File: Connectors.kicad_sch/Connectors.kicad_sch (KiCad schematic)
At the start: 4 parts, among them J1 I2C, J2 GPIO, J3 Serial, J4 ISCP

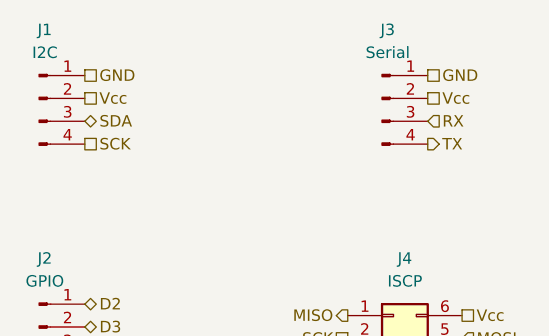
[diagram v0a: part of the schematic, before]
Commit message: Have added required symbols to the schematic sheets.
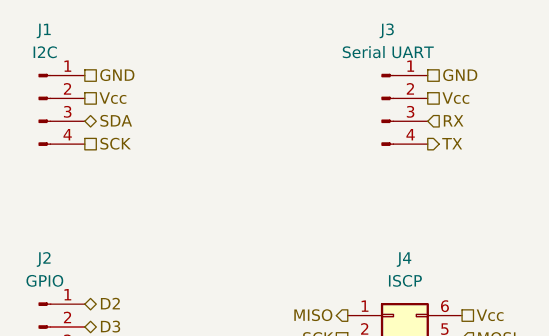
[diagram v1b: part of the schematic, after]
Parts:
- J3: value Serial -> Serial UART
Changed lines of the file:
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@@
 			)
 		)
-		(property "Value" "Serial"
+		(property "Value" "Serial UART"
 			(at 158.115 73.66 0)
 			(effects

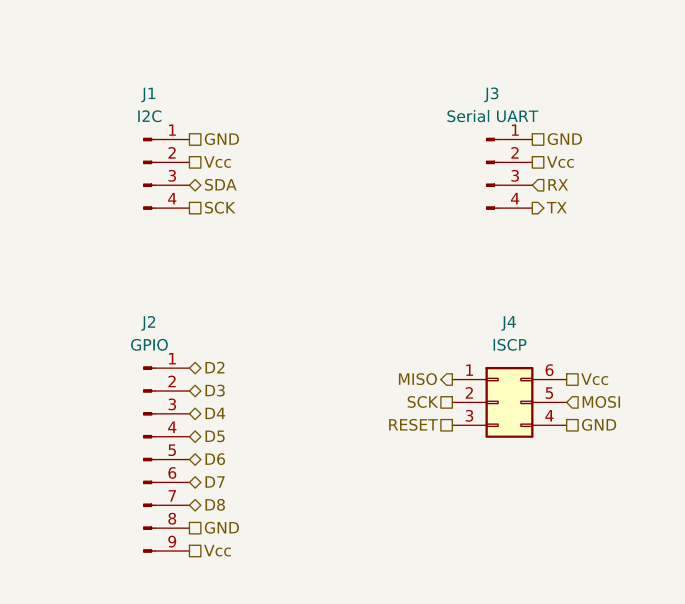
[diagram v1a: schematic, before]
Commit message: Added component values.
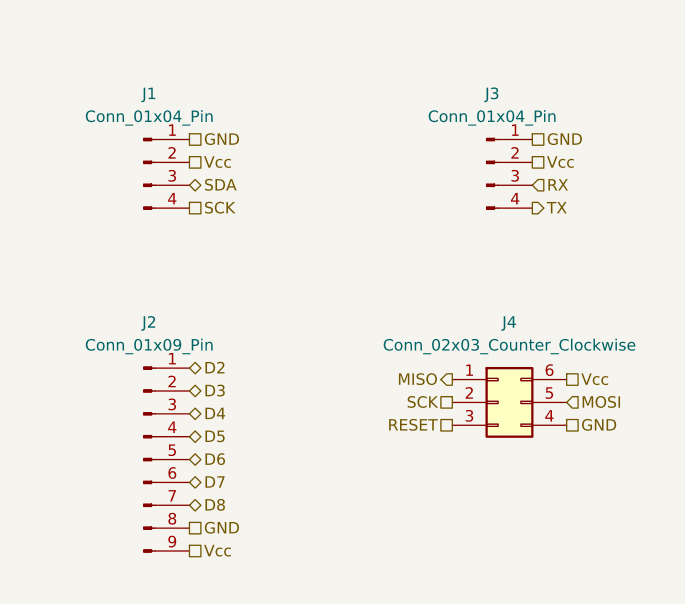
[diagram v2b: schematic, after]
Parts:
- J1: value I2C -> Conn_01x04_Pin
- J2: value GPIO -> Conn_01x09_Pin
- J3: value Serial UART -> Conn_01x04_Pin
- J4: value ISCP -> Conn_02x03_Counter_Clockwise
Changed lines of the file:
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@@
 	)
 	(symbol
+		(lib_name "Conn_02x03_Counter_Clockwise_1")
 		(lib_id "Connector_Generic:Conn_02x03_Counter_Clockwise")
 		(at 158.75 105.41 0)
@@
 			)
 		)
-		(property "Value" "ISCP"
+		(property "Value" "Conn_02x03_Counter_Clockwise"
 			(at 160.02 99.06 0)
 			(effects
@@
 			)
 		)
+		(pin "6"
+		)
+		(pin "3"
+		)
+		(pin "5"
+		)
+		(pin "1"
+		)
 		(pin "4"
 		)
-		(pin "5"
-		)
-		(pin "1"
-		)
 		(pin "2"
 		)
-		(pin "6"
-		)
-		(pin "3"
-		)
 		(instances
-			(project "KiCAD_Proj (MCU datalogger)"
+			(project ""
 				(path "/4bd39814-648a-43e5-9d59-9775154104be/332bdd2b-acd5-4556-89bc-1329fd5879e3"
 					(reference "J4")
@@
 	)
 	(symbol
-		(lib_name "Conn_01x04_Pin_1")
+		(lib_name "Conn_01x04_Pin_2")
 		(lib_id "Connector:Conn_01x04_Pin")
-		(at 130.81 74.93 0)
+		(at 157.48 78.74 0)
 		(unit 1)
 		(exclude_from_sim no)
@@
 		(on_board yes)
 		(dnp no)
+		(fields_autoplaced yes)
+		(property "Reference" "J3"
+			(at 158.115 71.12 0)
+			(effects
+				(font
+					(size 1.27 1.27)
+				)
+			)
+		)
+		(property "Value" "Conn_01x04_Pin"
+			(at 158.115 73.66 0)
+			(effects
+				(font
+					(size 1.27 1.27)
+				)
+			)
+		)
+		(property "Footprint" ""
+			(at 157.48 78.74 0)
+			(effects
+				(font
+					(size 1.27 1.27)
+				)
+				(hide yes)
+			)
+		)
+		(property "Datasheet" "~"
+			(at 157.48 78.74 0)
+			(effects
+				(font
+					(size 1.27 1.27)
+				)
+				(hide yes)
+			)
+		)
+		(property "Description" "Generic connector, single row, 01x04, script generated"
+			(at 157.48 78.74 0)
+			(effects
+				(font
+					(size 1.27 1.27)
+				)
+				(hide yes)
+			)
+		)
+		(pin "3"
+		)
+		(pin "2"
+		)
+		(pin "4"
+		)
+		(pin "1"
+		)
+		(instances
+			(project ""
+				(path "/4bd39814-648a-43e5-9d59-9775154104be/332bdd2b-acd5-4556-89bc-1329fd5879e3"
+					(reference "J3")
+					(unit 1)
+				)
+			)
+		)
+	)
+	(symbol
+		(lib_name "Conn_01x04_Pin_3")
+		(lib_id "Connector:Conn_01x04_Pin")
+		(at 119.38 78.74 0)
+		(unit 1)
+		(exclude_from_sim no)
+		(in_bom yes)
+		(on_board yes)
+		(dnp no)
+		(fields_autoplaced yes)
 		(property "Reference" "J1"
 			(at 120.015 71.12 0)
@@
 			)
 		)
-		(property "Value" "I2C"
+		(property "Value" "Conn_01x04_Pin"
 			(at 120.015 73.66 0)
 			(effects
@@
 			)
 		)
+		(pin "2"
+		)
 		(pin "1"
 		)
+		(pin "3"
+		)
 		(pin "4"
 		)
-		(pin "2"
-		)
-		(pin "3"
-		)
 		(instances
-			(project "KiCAD_Proj (MCU datalogger)"
+			(project ""
 				(path "/4bd39814-648a-43e5-9d59-9775154104be/332bdd2b-acd5-4556-89bc-1329fd5879e3"
 					(reference "J1")
@@
 	)
 	(symbol
+		(lib_name "Conn_01x09_Pin_1")
 		(lib_id "Connector:Conn_01x09_Pin")
 		(at 119.38 111.76 0)
@@
 			)
 		)
-		(property "Value" "GPIO"
+		(property "Value" "Conn_01x09_Pin"
 			(at 120.015 99.06 0)
 			(effects
@@
 			)
 		)
+		(property "Purpose" ""
+			(at 119.38 111.76 0)
+			(effects
+				(font
+					(size 1.27 1.27)
+				)
+			)
+		)
+		(pin "6"
+		)
+		(pin "1"
+		)
+		(pin "2"
+		)
+		(pin "7"
+		)
+		(pin "4"
+		)
 		(pin "5"
 		)
@@
 		(pin "8"
 		)
-		(pin "2"
-		)
-		(pin "6"
-		)
-		(pin "4"
-		)
 		(pin "9"
 		)
-		(pin "7"
-		)
-		(pin "1"
-		)
 		(instances
-			(project "KiCAD_Proj (MCU datalogger)"
+			(project ""
 				(path "/4bd39814-648a-43e5-9d59-9775154104be/332bdd2b-acd5-4556-89bc-1329fd5879e3"
 					(reference "J2")
 					(unit 1)
 				)
-			)
-		)
-	)
-	(symbol
-		(lib_id "Connector:Conn_01x04_Pin")
-		(at 157.48 78.74 0)
-		(unit 1)
-		(exclude_from_sim no)
-		(in_bom yes)
-		(on_board yes)
-		(dnp no)
-		(fields_autoplaced yes)
-		(property "Reference" "J3"
-			(at 158.115 71.12 0)
-			(effects
-				(font
-					(size 1.27 1.27)
-				)
-			)
-		)
-		(property "Value" "Serial UART"
-			(at 158.115 73.66 0)
-			(effects
-				(font
-					(size 1.27 1.27)
-				)
-			)
-		)
-		(property "Footprint" ""
-			(at 157.48 78.74 0)
-			(effects
-				(font
-					(size 1.27 1.27)
-				)
-				(hide yes)
-			)
-		)
-		(property "Datasheet" "~"
-			(at 157.48 78.74 0)
-			(effects
-				(font
-					(size 1.27 1.27)
-				)
-				(hide yes)
-			)
-		)
-		(property "Description" "Generic connector, single row, 01x04, script generated"
-			(at 157.48 78.74 0)
-			(effects
-				(font
-					(size 1.27 1.27)
-				)
-				(hide yes)
-			)
-		)
-		(pin "1"
-		)
-		(pin "4"
-		)
-		(pin "2"
-		)
-		(pin "3"
-		)
-		(instances
-			(project "KiCAD_Proj (MCU datalogger)"
-				(path "/4bd39814-648a-43e5-9d59-9775154104be/332bdd2b-acd5-4556-89bc-1329fd5879e3"
-					(reference "J3")
-					(unit 1)
-				)

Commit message: Allocated GND and Vcc nets to the Power net class.
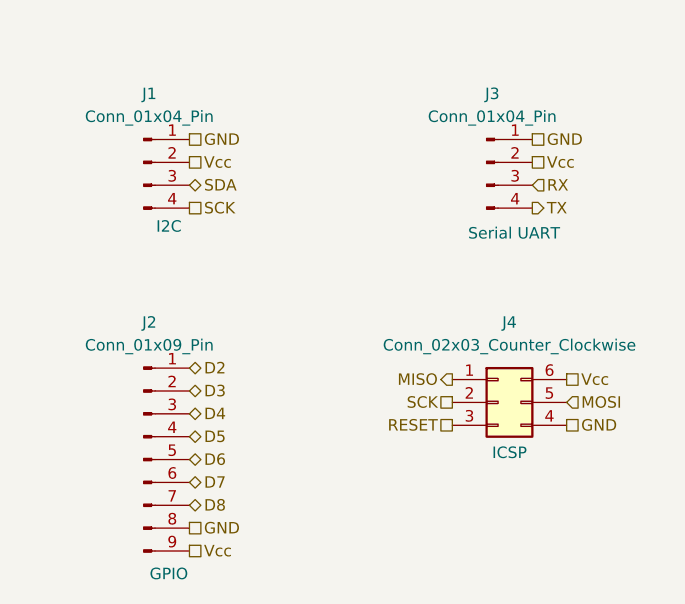
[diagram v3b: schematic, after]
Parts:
- J1: Purpose (none) -> I2C
- J2: Purpose (none) -> GPIO
- J3: Purpose (none) -> Serial UART
- J4: Purpose (none) -> ICSP
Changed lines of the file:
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@@
 		(on_board yes)
 		(dnp no)
-		(fields_autoplaced yes)
 		(property "Reference" "J4"
 			(at 160.02 96.52 0)
@@
 				)
 				(hide yes)
+			)
+		)
+		(property "Purpose" "ICSP"
+			(at 160.02 110.998 0)
+			(effects
+				(font
+					(size 1.27 1.27)
+				)
 			)
 		)
@@
 		(on_board yes)
 		(dnp no)
-		(fields_autoplaced yes)
 		(property "Reference" "J3"
 			(at 158.115 71.12 0)
@@
 				)
 				(hide yes)
+			)
+		)
+		(property "Purpose" "Serial UART"
+			(at 160.528 86.614 0)
+			(effects
+				(font
+					(size 1.27 1.27)
+				)
 			)
 		)
@@
 		(on_board yes)
 		(dnp no)
-		(fields_autoplaced yes)
 		(property "Reference" "J1"
 			(at 120.015 71.12 0)
@@
 				)
 				(hide yes)
+			)
+		)
+		(property "Purpose" "I2C"
+			(at 122.174 85.852 0)
+			(effects
+				(font
+					(size 1.27 1.27)
+				)
 			)
 		)
@@
 		(on_board yes)
 		(dnp no)
-		(fields_autoplaced yes)
 		(property "Reference" "J2"
 			(at 120.015 96.52 0)
@@
 			)
 		)
-		(property "Purpose" ""
-			(at 119.38 111.76 0)
-			(effects
-				(font
+		(property "Purpose" "GPIO"
+			(at 122.174 124.46 0)
+			(effects
+				(font

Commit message: Added required symbols to schematic sheets and connectors
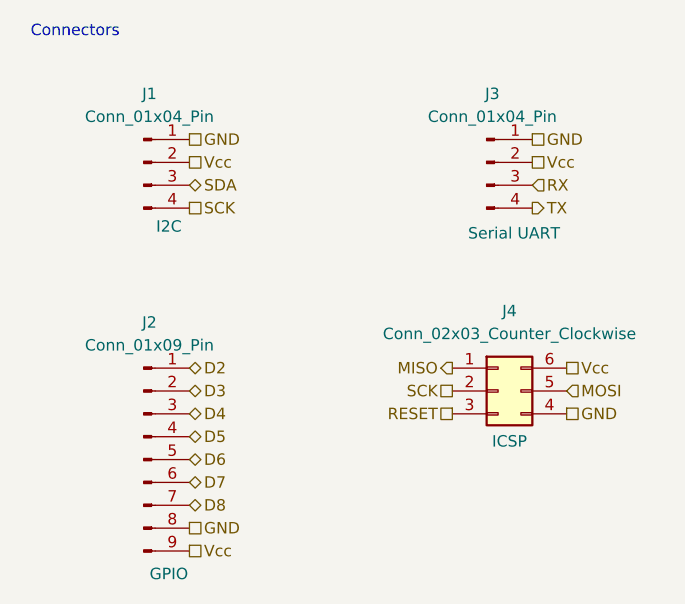
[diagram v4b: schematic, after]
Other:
- note added: "Connectors"
- moved on the sheet: J4
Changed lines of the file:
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@@
 	(generator_version "9.0")
 	(paper "A4")
+	(text "Connectors"
+		(exclude_from_sim no)
+		(at 111.76 64.262 0)
+		(effects
+			(font
+				(size 1.27 1.27)
+			)
+		)
+	)
 	(hierarchical_label "D3"
 		(shape tri_state)
@@
 	(hierarchical_label "MISO"
 		(shape output)
-		(at 153.67 102.87 180)
+		(at 153.67 101.6 180)
 		(effects
 			(font
@@
 	(hierarchical_label "GND"
 		(shape passive)
-		(at 166.37 107.95 0)
+		(at 166.37 106.68 0)
 		(effects
 			(font
@@
 	(hierarchical_label "RESET"
 		(shape passive)
-		(at 153.67 107.95 180)
+		(at 153.67 106.68 180)
 		(effects
 			(font
@@
 	(hierarchical_label "Vcc"
 		(shape passive)
-		(at 166.37 102.87 0)
+		(at 166.37 101.6 0)
 		(effects
 			(font
@@
 	(hierarchical_label "SCK"
 		(shape passive)
-		(at 153.67 105.41 180)
+		(at 153.67 104.14 180)
 		(effects
 			(font
@@
 	(hierarchical_label "MOSI"
 		(shape input)
-		(at 166.37 105.41 0)
+		(at 166.37 104.14 0)
 		(effects
 			(font
@@
 			)
 			(justify left)
+		)
+	)
+	(rule_area
+		(polyline
+			(pts
+				(xy 106.68 66.04) (xy 179.07 66.04) (xy 179.07 130.81) (xy 106.68 130.81)
+			)
+			(stroke
+				(width 0)
+				(type dash)
+			)
+			(fill
+				(type none)
+			)
 		)
 	)
@@
 		(lib_name "Conn_02x03_Counter_Clockwise_1")
 		(lib_id "Connector_Generic:Conn_02x03_Counter_Clockwise")
-		(at 158.75 105.41 0)
+		(at 158.75 104.14 0)
 		(unit 1)
 		(exclude_from_sim no)
@@
 		(dnp no)
 		(property "Reference" "J4"
-			(at 160.02 96.52 0)
+			(at 160.02 95.25 0)
 			(effects
 				(font
@@
 		)
 		(property "Value" "Conn_02x03_Counter_Clockwise"
-			(at 160.02 99.06 0)
+			(at 160.02 97.79 0)
 			(effects
 				(font
@@
 		)
 		(property "Footprint" ""
-			(at 158.75 105.41 0)
+			(at 158.75 104.14 0)
 			(effects
 				(font
@@
 		)
 		(property "Datasheet" "~"
-			(at 158.75 105.41 0)
+			(at 158.75 104.14 0)
 			(effects
 				(font
@@
 		)
 		(property "Description" "Generic connector, double row, 02x03, counter clockwise pin numbering scheme (similar to DIP package numbering), script generated (kicad-library-utils/schlib/autogen/connector/)"
-			(at 158.75 105.41 0)
+			(at 158.75 104.14 0)
 			(effects
 				(font
@@
 		)
 		(property "Purpose" "ICSP"
-			(at 160.02 110.998 0)
-			(effects
-				(font
+			(at 160.02 109.728 0)
+			(effects
+				(font

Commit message: Routing sans GND Vcc Complete.
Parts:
- J1, J3: footprint (none) -> Connector_PinHeader_2.54mm:PinHeader_1x04_P2.54mm_Vertical
- J2: footprint (none) -> Connector_PinHeader_2.54mm:PinHeader_1x09_P2.54mm_Vertical
- J4: footprint (none) -> Connector_PinHeader_2.54mm:PinHeader_2x03_P2.54mm_Vertical
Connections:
- net GND: now also J4.6 (Pin_6); no longer J4.4 (Pin_4)
- net MOSI: now also J4.4 (Pin_4); no longer J4.5 (Pin_5)
- net RESET: now also J4.5 (Pin_5); no longer J4.3 (Pin_3)
- net SCK: now also J4.3 (Pin_3); no longer J4.2 (Pin_2)
- net Vcc: now also J4.2 (Pin_2); no longer J4.6 (Pin_6)
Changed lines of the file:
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@@
 	(hierarchical_label "GND"
 		(shape passive)
-		(at 166.37 106.68 0)
+		(at 166.37 101.6 0)
 		(effects
 			(font
@@
 	(hierarchical_label "RESET"
 		(shape passive)
-		(at 153.67 106.68 180)
+		(at 166.37 104.14 0)
+		(effects
+			(font
+				(size 1.27 1.27)
+			)
+			(justify left)
+		)
+	)
+	(hierarchical_label "Vcc"
+		(shape passive)
+		(at 153.67 104.14 180)
 		(effects
 			(font
@@
 			)
 			(justify right)
-		)
-	)
-	(hierarchical_label "Vcc"
-		(shape passive)
-		(at 166.37 101.6 0)
-		(effects
-			(font
-				(size 1.27 1.27)
-			)
-			(justify left)
 		)
 	)
@@
 	(hierarchical_label "SCK"
 		(shape passive)
-		(at 153.67 104.14 180)
+		(at 153.67 106.68 180)
 		(effects
 			(font
@@
 	(hierarchical_label "MOSI"
 		(shape input)
-		(at 166.37 104.14 0)
+		(at 166.37 106.68 0)
 		(effects
 			(font
@@
 		(polyline
 			(pts
-				(xy 106.68 66.04) (xy 179.07 66.04) (xy 179.07 130.81) (xy 106.68 130.81)
+				(xy 106.68 66.04) (xy 179.07 66.04) (xy 178.435 129.54) (xy 106.045 129.54)
 			)
 			(stroke
@@
 			)
 		)
-		(property "Footprint" ""
+		(property "Footprint" "Connector_PinHeader_2.54mm:PinHeader_2x03_P2.54mm_Vertical"
 			(at 158.75 104.14 0)
 			(effects
@@
 			)
 		)
-		(property "Footprint" ""
+		(property "Footprint" "Connector_PinHeader_2.54mm:PinHeader_1x04_P2.54mm_Vertical"
 			(at 157.48 78.74 0)
 			(effects
@@
 			)
 		)
-		(property "Footprint" ""
+		(property "Footprint" "Connector_PinHeader_2.54mm:PinHeader_1x04_P2.54mm_Vertical"
 			(at 119.38 78.74 0)
 			(effects
@@
 			)
 		)
-		(property "Footprint" ""
+		(property "Footprint" "Connector_PinHeader_2.54mm:PinHeader_1x09_P2.54mm_Vertical"
 			(at 119.38 111.76 0)
 			(effects

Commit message: Fixed bugs in schematic.
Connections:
- net SCK: no longer J1.4 (Pin_4)
- new net SCL: J1.4 (Pin_4)
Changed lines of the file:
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@@
 		)
 	)
-	(hierarchical_label "SCK"
+	(hierarchical_label "SCL"
 		(shape passive)
 		(at 124.46 83.82 0)
@@
 		(polyline
 			(pts
-				(xy 106.68 66.04) (xy 179.07 66.04) (xy 178.435 129.54) (xy 106.045 129.54)
+				(xy 106.68 66.04) (xy 179.07 66.04) (xy 179.07 129.54) (xy 106.68 129.54)
 			)
 			(stroke
-				(width 0)
-				(type dash)
+				(width 0.254)
+				(type solid)
+				(color 0 0 139 1)
 			)
 			(fill
